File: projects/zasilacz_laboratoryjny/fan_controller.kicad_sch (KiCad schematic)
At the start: 38 parts, among them J201 OFF_BOARD, J202 PWR, J203 OFF_BOARD, J204 GND, J205 OFF_BOARD, J206 FANL+, J207 FANL-, J208 OFF_BOARD, J209 TSENSE1, J210 OFF_BOARD, J211 OFF_BOARD, J212 TSENSE2, J213 FAN+, J214 OFF_BOARD, J215 OFF_BOARD, J216 FAN−, M201 Fan_DC, P201 10kΩ, T201 BC557, T202 BC557, T203 2N7000, U201 78L12

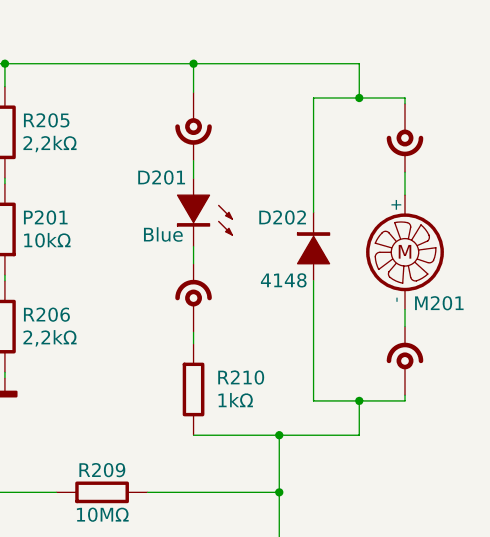
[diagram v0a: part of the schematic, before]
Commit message: project updates (kicad upgrade related?)
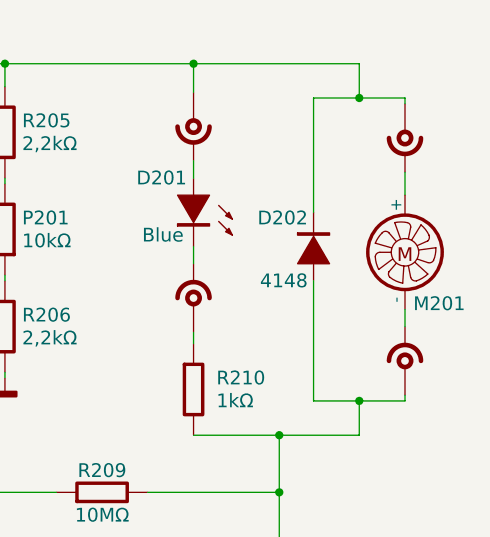
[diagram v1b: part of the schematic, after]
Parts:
- M201: symbol *Custom_Generic:Fan_DC -> Custom_Generic:Fan_DC
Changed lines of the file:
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@@
     )
   )
-  (symbol (lib_id "*Custom_Generic:Fan_DC") (at 227.965 74.295 0) (mirror y) (unit 1)
+  (symbol (lib_id "Custom_Generic:Fan_DC") (at 227.965 74.295 0) (mirror y) (unit 1)
     (in_bom yes) (on_board no) (dnp no)
     (property "Reference" "M201" (at 231.775 80.01 0)
